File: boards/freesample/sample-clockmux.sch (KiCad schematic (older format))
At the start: 26 parts, among them J15 SMA, J16 SMA, U11 PI6C59S6005, U12 PI6C59S6005

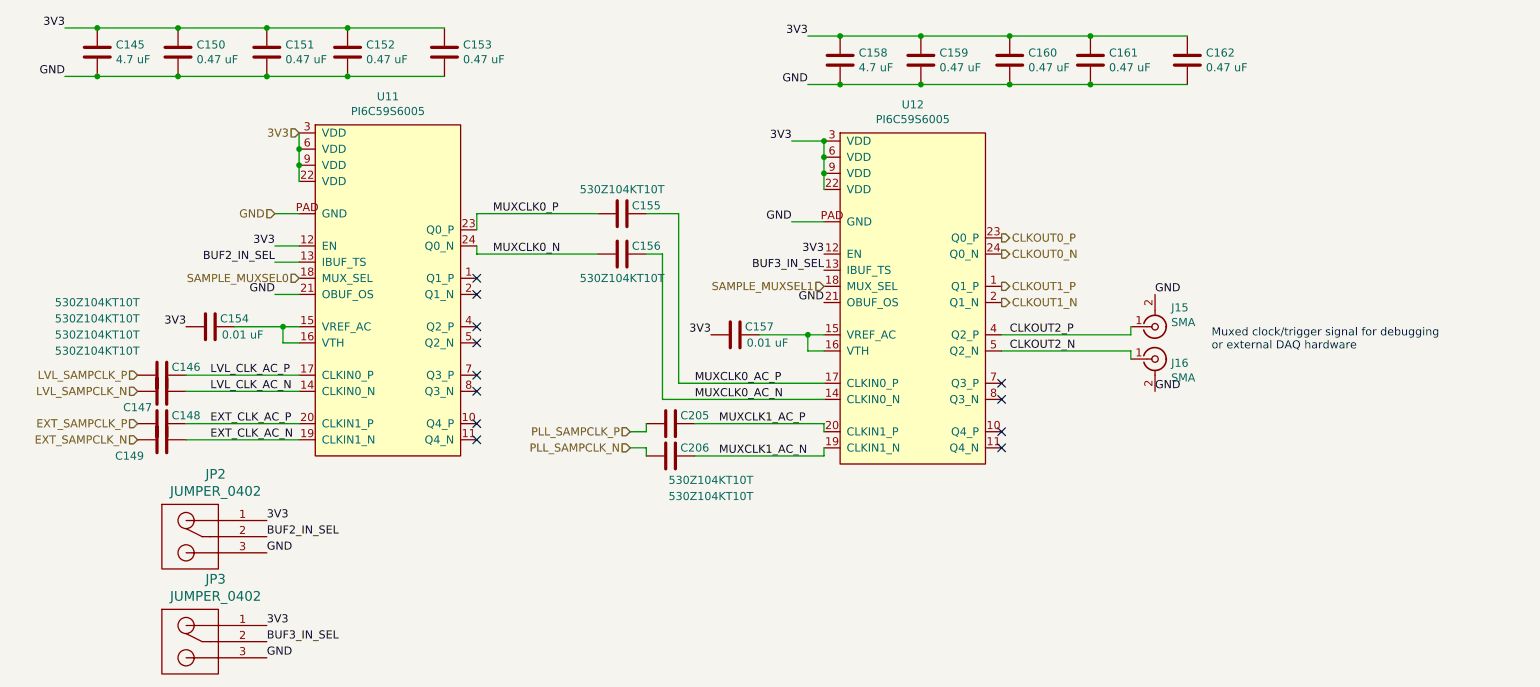
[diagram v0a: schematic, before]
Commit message: Added more test points. Started picking packages for passives. Continued schematic review.
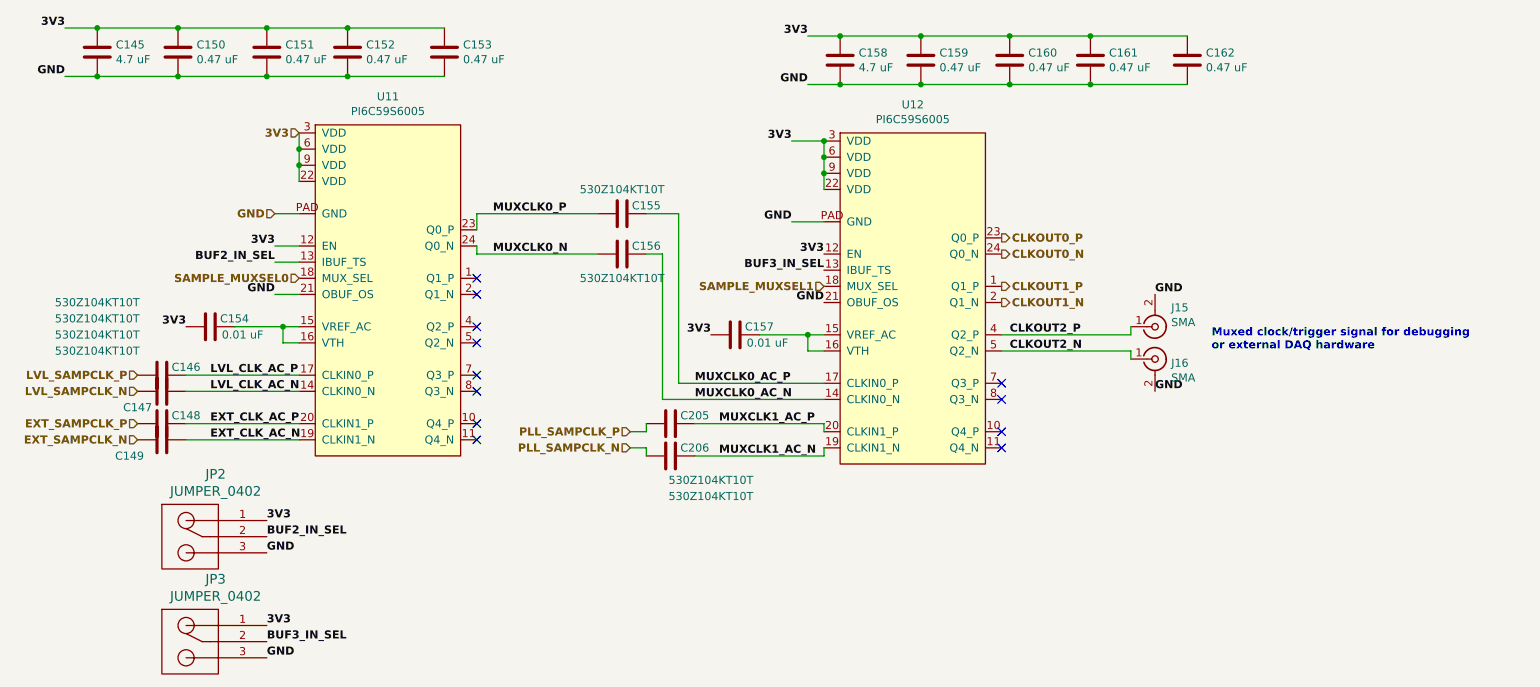
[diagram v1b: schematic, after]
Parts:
- C145, C158: footprint (none) -> azonenberg_pcb:EIA_0603_CAP_NOSILK
- C146, C147, C148, C149, C155, C156, C205, C206: footprint (none) -> azonenberg_pcb:EIA_0201_CAP_NOSILK
- C150, C151, C152, C153, C154, C157, C159, C160, C161, C162: footprint (none) -> azonenberg_pcb:EIA_0402_CAP_NOSILK
- J15, J16: footprint (none) -> azonenberg_pcb:CONN_SMA_EDGE_SAMTEC_SMA_J_P_H_ST_EM1
- JP2, JP3: footprint (none) -> azonenberg_pcb:EIA_0402_JUMPER
- U11, U12: footprint (none) -> azonenberg_pcb:QFN_24_0.5MM_4x4MM

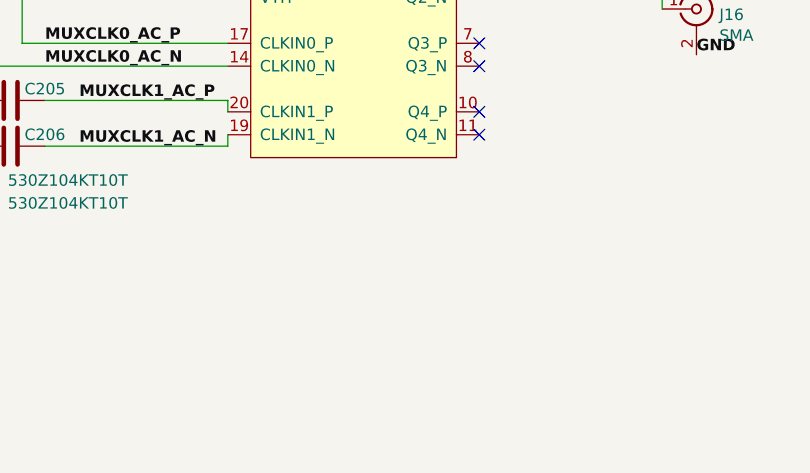
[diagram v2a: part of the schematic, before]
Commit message: Continued design review. Changed termination on DFFs to 1V8. Added some pull resistors to keep DFFs in reset during boot.
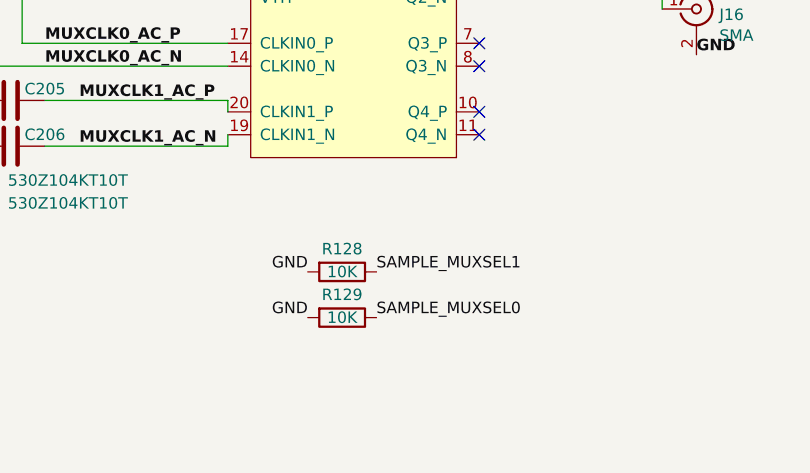
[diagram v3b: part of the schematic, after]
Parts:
- added R128, R129: 10K, azonenberg_pcb:EIA_0402_RES_NOSILK, symbol device:R
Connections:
- net GND: now also R128.2, R129.2
- net SAMPLE_MUXSEL0: now also R129.1
- net SAMPLE_MUXSEL1: now also R128.1
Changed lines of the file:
@@
 Sheet 11 12
 Title "FREESAMPLE Oscilloscope"
-Date "2019-03-16"
+Date "2019-03-17"
 Rev "0.1"
 Comp "Andrew D. Zonenberg / Antikernel Labs"
@@
 Text Notes 8000 2650 0    50   ~ 6
 Muxed clock/trigger signal for debugging\nor external DAQ hardware
+Text Label 6250 3850 0    50   ~ 0
+SAMPLE_MUXSEL1
+$Comp
+L device:R R128
+U 1 1 5D06BEC1
+P 6100 3850
+F 0 "R128" V 6000 3850 50  0000 C CNN
+F 1 "10K" V 6100 3850 50  0000 C CNN
+F 2 "azonenberg_pcb:EIA_0402_RES_NOSILK" V 6030 3850 50  0001 C CNN
+F 3 "" H 6100 3850 50  0001 C CNN
+	1    6100 3850
+	0    1    1    0
+$EndComp
+Text Label 5950 3850 2    50   ~ 0
+GND
+Text Label 6250 4050 0    50   ~ 0
+SAMPLE_MUXSEL0
+$Comp
+L device:R R129
+U 1 1 5D06DEDA
+P 6100 4050
+F 0 "R129" V 6000 4050 50  0000 C CNN
+F 1 "10K" V 6100 4050 50  0000 C CNN
+F 2 "azonenberg_pcb:EIA_0402_RES_NOSILK" V 6030 4050 50  0001 C CNN
+F 3 "" H 6100 4050 50  0001 C CNN
+	1    6100 4050
+	0    1    1    0
+$EndComp
+Text Label 5950 4050 2    50   ~ 0
+GND
 $EndSCHEMATC

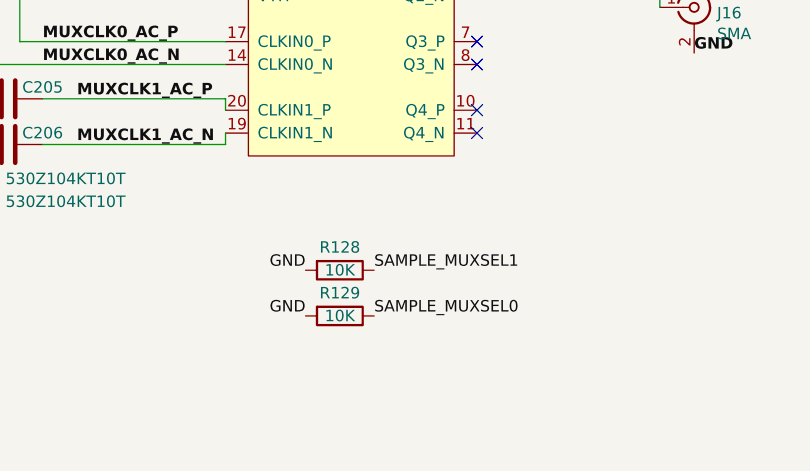
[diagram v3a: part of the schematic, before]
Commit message: Added fiducials
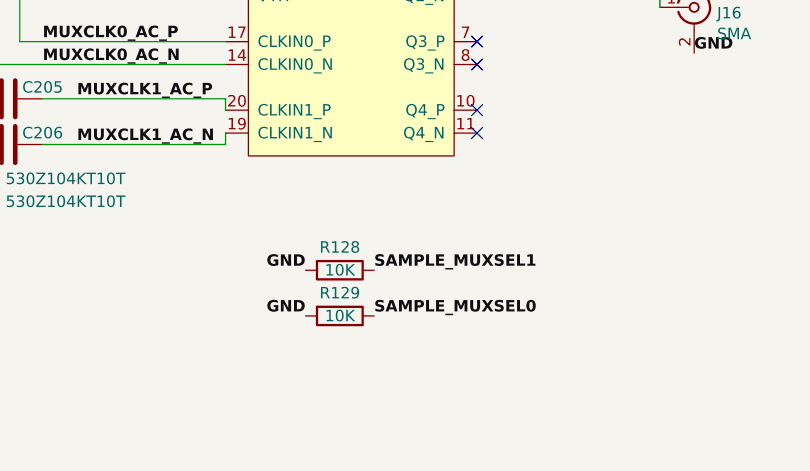
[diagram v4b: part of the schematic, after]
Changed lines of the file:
@@
 Text Notes 8000 2650 0    50   ~ 6
 Muxed clock/trigger signal for debugging\nor external DAQ hardware
-Text Label 6250 3850 0    50   ~ 0
+Text Label 6250 3850 0    50   ~ 6
 SAMPLE_MUXSEL1
 $Comp
@@
 	0    1    1    0
 $EndComp
-Text Label 5950 3850 2    50   ~ 0
+Text Label 5950 3850 2    50   ~ 6
 GND
-Text Label 6250 4050 0    50   ~ 0
+Text Label 6250 4050 0    50   ~ 6
 SAMPLE_MUXSEL0
 $Comp
@@
 	0    1    1    0
 $EndComp
-Text Label 5950 4050 2    50   ~ 0
+Text Label 5950 4050 2    50   ~ 6
 GND
 $EndSCHEMATC

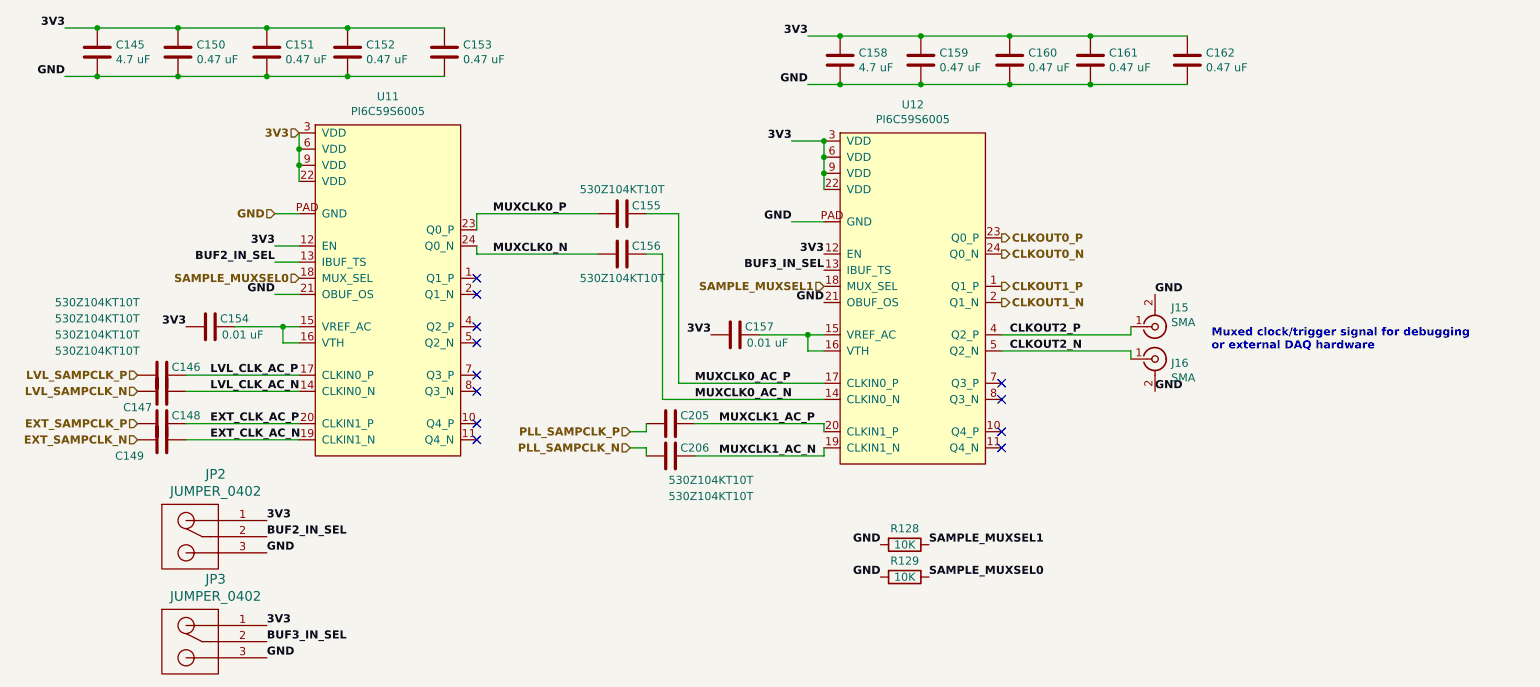
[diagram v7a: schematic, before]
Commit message: Tweaks to PLL and CDR layout, swapped a few signals around. Began work on level trigger and ADC layout.
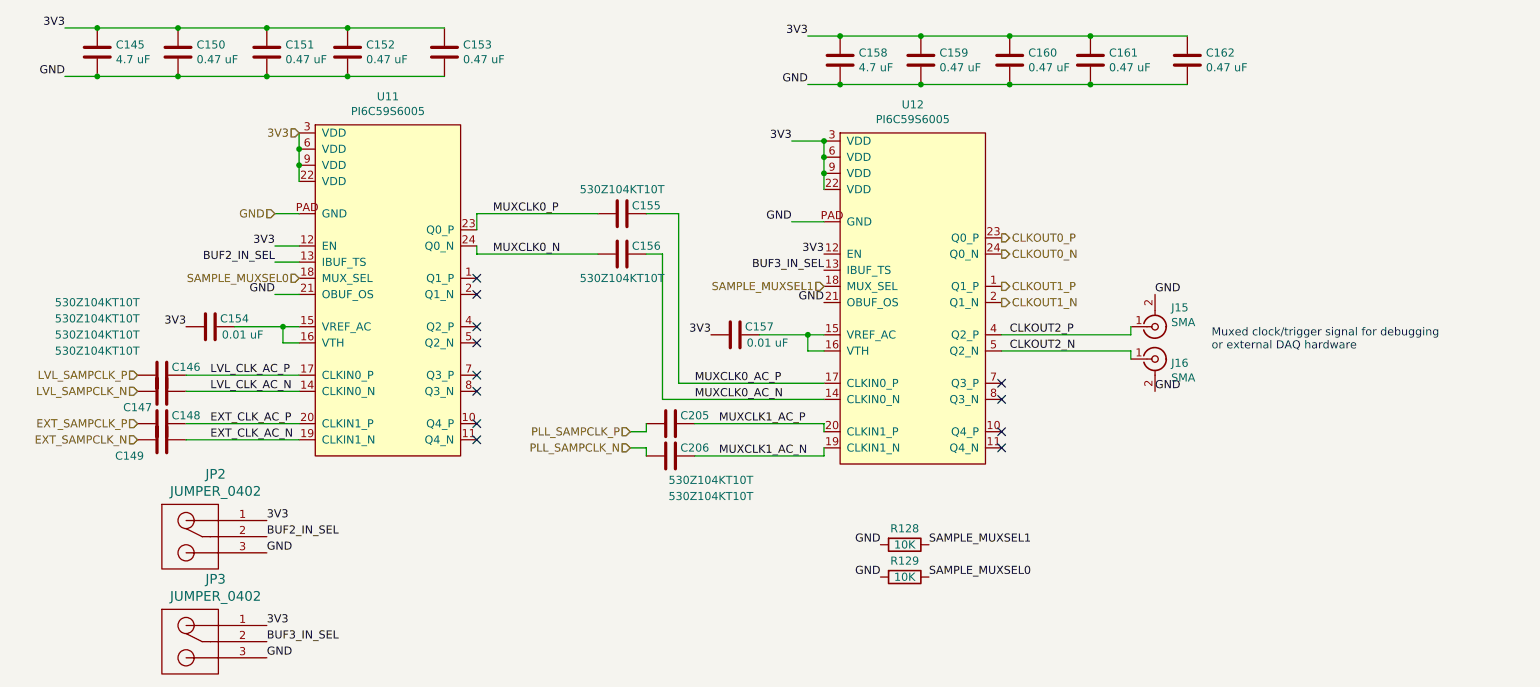
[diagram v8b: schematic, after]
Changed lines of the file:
@@
 Comment4 ""
 $EndDescr
-Text HLabel 4400 3150 0    50   Input ~ 10
+Text HLabel 4400 3150 0    50   Input ~ 0
 PLL_SAMPCLK_P
-Text HLabel 4400 3250 0    50   Input ~ 10
+Text HLabel 4400 3250 0    50   Input ~ 0
 PLL_SAMPCLK_N
-Text HLabel 1350 3200 0    50   Input ~ 10
+Text HLabel 1350 3200 0    50   Input ~ 0
 EXT_SAMPCLK_N
-Text HLabel 1350 2800 0    50   Input ~ 10
+Text HLabel 1350 2800 0    50   Input ~ 0
 LVL_SAMPCLK_P
-Text HLabel 1350 2900 0    50   Input ~ 10
+Text HLabel 1350 2900 0    50   Input ~ 0
 LVL_SAMPCLK_N
-Text HLabel 2350 2200 0    50   Input ~ 10
+Text HLabel 2350 2200 0    50   Input ~ 0
 SAMPLE_MUXSEL0
-Text HLabel 5600 2250 0    50   Input ~ 10
+Text HLabel 5600 2250 0    50   Input ~ 0
 SAMPLE_MUXSEL1
 $Comp
@@
 	1    0    0    -1
 $EndComp
-Text HLabel 6700 1950 2    50   Output ~ 10
+Text HLabel 6700 1950 2    50   Output ~ 0
 CLKOUT0_P
-Text HLabel 6700 2050 2    50   Output ~ 10
+Text HLabel 6700 2050 2    50   Output ~ 0
 CLKOUT0_N
-Text HLabel 6700 2250 2    50   Output ~ 10
+Text HLabel 6700 2250 2    50   Output ~ 0
 CLKOUT1_P
-Text HLabel 6700 2350 2    50   Output ~ 10
+Text HLabel 6700 2350 2    50   Output ~ 0
 CLKOUT1_N
-Text HLabel 2350 1300 0    50   Input ~ 10
-3V3
-Text HLabel 2200 1800 0    50   Input ~ 10
+Text HLabel 2350 1300 0    50   Input ~ 0
+3V3
+Text HLabel 2200 1800 0    50   Input ~ 0
 GND
 Wire Wire Line
@@
 Wire Wire Line
 	1600 950  1100 950
-Text Label 900  650  2    50   ~ 10
+Text Label 900  650  2    50   ~ 0
 3V3
 Wire Wire Line
 	900  650  1100 650
 Connection ~ 1100 650
-Text Label 900  950  2    50   ~ 10
+Text Label 900  950  2    50   ~ 0
 GND
 Wire Wire Line
@@
 	3250 950  2650 950
 Connection ~ 2650 950
-Text Label 2200 2000 2    50   ~ 10
+Text Label 2200 2000 2    50   ~ 0
 3V3
 Wire Wire Line
 	2200 2000 2350 2000
-Text Label 2200 2100 2    50   ~ 10
+Text Label 2200 2100 2    50   ~ 0
 BUF2_IN_SEL
 Wire Wire Line
@@
 	1    0    0    -1
 $EndComp
-Text Label 2150 3800 0    50   ~ 10
+Text Label 2150 3800 0    50   ~ 0
 BUF2_IN_SEL
-Text Label 2150 3700 0    50   ~ 10
-3V3
-Text Label 2150 3900 0    50   ~ 10
-GND
-Text Label 2200 2300 2    50   ~ 10
+Text Label 2150 3700 0    50   ~ 0
+3V3
+Text Label 2150 3900 0    50   ~ 0
+GND
+Text Label 2200 2300 2    50   ~ 0
 GND
 Wire Wire Line
@@
 	0    1    -1   0
 $EndComp
-Text Label 1800 3100 0    50   ~ 10
+Text Label 1800 3100 0    50   ~ 0
 EXT_CLK_AC_P
-Text Label 1800 3200 0    50   ~ 10
+Text Label 1800 3200 0    50   ~ 0
 EXT_CLK_AC_N
 Wire Wire Line
@@
 Wire Wire Line
 	2350 3200 1650 3200
-Text Label 1800 2800 0    50   ~ 10
+Text Label 1800 2800 0    50   ~ 0
 LVL_CLK_AC_P
 $Comp
@@
 	0    1    -1   0
 $EndComp
-Text Label 1800 2900 0    50   ~ 10
+Text Label 1800 2900 0    50   ~ 0
 LVL_CLK_AC_N
 Wire Wire Line
@@
 Wire Wire Line
 	2350 2900 1650 2900
-Text HLabel 1350 3100 0    50   Input ~ 10
+Text HLabel 1350 3100 0    50   Input ~ 0
 EXT_SAMPCLK_P
 $Comp
@@
 	0    1    -1   0
 $EndComp
-Text Label 1650 2500 2    50   ~ 10
+Text Label 1650 2500 2    50   ~ 0
 3V3
 Wire Wire Line
 	1950 2500 2250 2500
 Connection ~ 2250 2500
-Text Label 5400 1350 2    50   ~ 10
+Text Label 5400 1350 2    50   ~ 0
 3V3
 Wire Wire Line
@@
 Wire Wire Line
 	5600 1550 5600 1650
-Text Label 5400 1850 2    50   ~ 10
+Text Label 5400 1850 2    50   ~ 0
 GND
 Wire Wire Line
@@
 Wire Wire Line
 	6200 1000 5700 1000
-Text Label 5500 700  2    50   ~ 10
+Text Label 5500 700  2    50   ~ 0
 3V3
 Wire Wire Line
 	5500 700  5700 700
 Connection ~ 5700 700
-Text Label 5500 1000 2    50   ~ 10
+Text Label 5500 1000 2    50   ~ 0
 GND
 Wire Wire Line
@@
 	7850 1000 7250 1000
 Connection ~ 7250 1000
-Text Label 5600 2050 2    50   ~ 10
-3V3
-Text Label 5600 2150 2    50   ~ 10
+Text Label 5600 2050 2    50   ~ 0
+3V3
+Text Label 5600 2150 2    50   ~ 0
 BUF3_IN_SEL
 $Comp
@@
 	1    0    0    -1
 $EndComp
-Text Label 2150 4450 0    50   ~ 10
+Text Label 2150 4450 0    50   ~ 0
 BUF3_IN_SEL
-Text Label 2150 4350 0    50   ~ 10
-3V3
-Text Label 2150 4550 0    50   ~ 10
-GND
-Text Label 5600 2350 2    50   ~ 10
+Text Label 2150 4350 0    50   ~ 0
+3V3
+Text Label 2150 4550 0    50   ~ 0
+GND
+Text Label 5600 2350 2    50   ~ 0
 GND
 NoConn ~ 6700 2850
@@
 Wire Wire Line
 	4600 2950 5600 2950
-Text Label 4800 2850 0    50   ~ 10
+Text Label 4800 2850 0    50   ~ 0
 MUXCLK0_AC_P
-Text Label 4800 2950 0    50   ~ 10
+Text Label 4800 2950 0    50   ~ 0
 MUXCLK0_AC_N
 Wire Wire Line
@@
 Wire Wire Line
 	3450 2050 4200 2050
-Text Label 3550 1800 0    50   ~ 10
+Text Label 3550 1800 0    50   ~ 0
 MUXCLK0_P
-Text Label 3550 2050 0    50   ~ 10
+Text Label 3550 2050 0    50   ~ 0
 MUXCLK0_N
 Wire Wire Line
@@
 	0    1    -1   0
 $EndComp
-Text Label 4900 2550 2    50   ~ 10
+Text Label 4900 2550 2    50   ~ 0
 3V3
 Wire Wire Line
@@
 Wire Wire Line
 	5600 3300 5600 3250
-Text Label 4950 3100 0    50   ~ 10
+Text Label 4950 3100 0    50   ~ 0
 MUXCLK1_AC_P
-Text Label 4950 3300 0    50   ~ 10
+Text Label 4950 3300 0    50   ~ 0
 MUXCLK1_AC_N
 $Comp
@@
 Wire Wire Line
 	7500 2650 7500 2700
-Text Label 7650 2300 0    50   ~ 10
-GND
-Text Label 7650 2900 0    50   ~ 10
-GND
-Text Label 6750 2550 0    50   ~ 10
+Text Label 7650 2300 0    50   ~ 0
+GND
+Text Label 7650 2900 0    50   ~ 0
+GND
+Text Label 6750 2550 0    50   ~ 0
 CLKOUT2_P
-Text Label 6750 2650 0    50   ~ 10
+Text Label 6750 2650 0    50   ~ 0
 CLKOUT2_N
-Text Notes 8000 2650 0    50   ~ 10
+Text Notes 8000 2650 0    50   ~ 0
 Muxed clock/trigger signal for debugging\nor external DAQ hardware
-Text Label 6250 3850 0    50   ~ 10
+Text Label 6250 3850 0    50   ~ 0
 SAMPLE_MUXSEL1
 $Comp
@@
 	0    1    1    0
 $EndComp
-Text Label 5950 3850 2    50   ~ 10
-GND
-Text Label 6250 4050 0    50   ~ 10
+Text Label 5950 3850 2    50   ~ 0
+GND
+Text Label 6250 4050 0    50   ~ 0
 SAMPLE_MUXSEL0
 $Comp
@@
 	0    1    1    0
 $EndComp
-Text Label 5950 4050 2    50   ~ 10
+Text Label 5950 4050 2    50   ~ 0
 GND
 $EndSCHEMATC
